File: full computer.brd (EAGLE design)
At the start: 99.9 x 90.2 mm, 74 parts, among them IC2 74HC541N, IC3 74HC573N, IC4 74HC04N, Q1 IRF9530, X1 1503_08

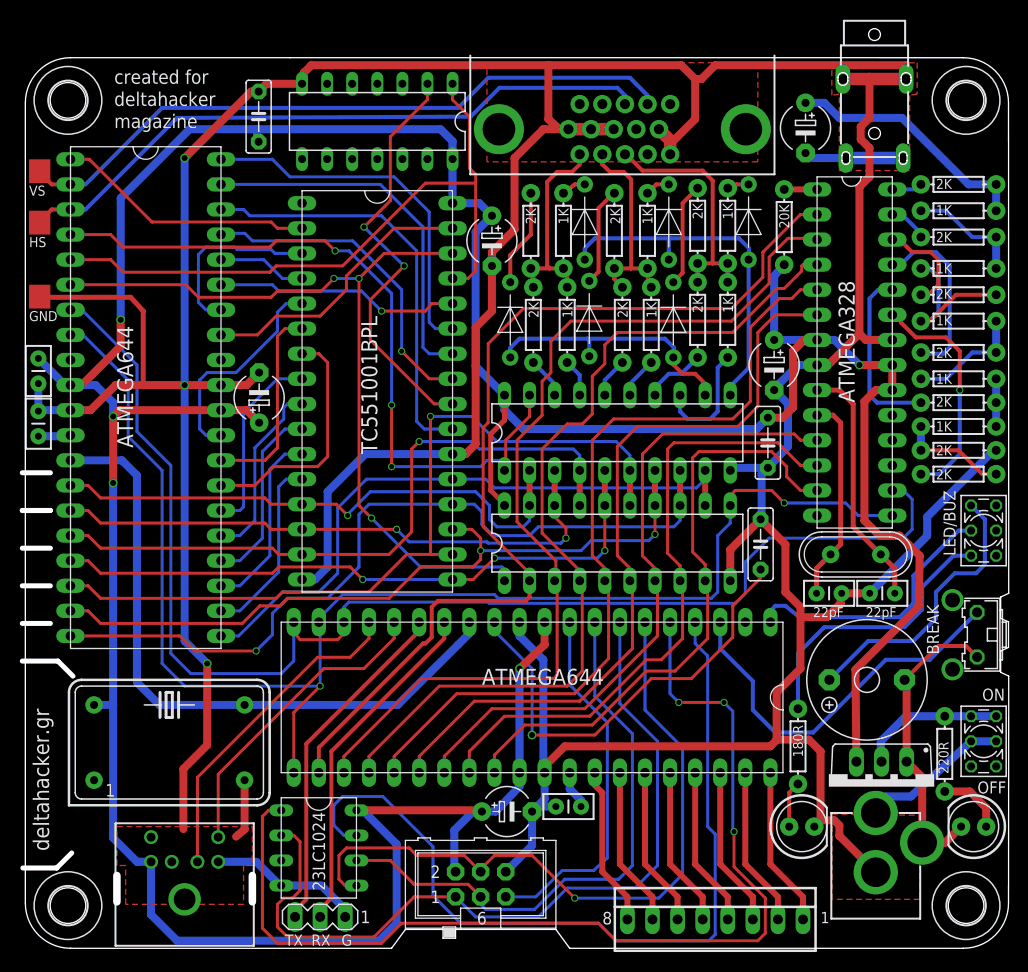
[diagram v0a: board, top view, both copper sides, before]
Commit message: thiner and shorter traces for clock signals, better position for GPIO and SERIAL, schematic clean up
Signed-off-by: Panagiotis Varelas <varelaspanos@gmail.com>
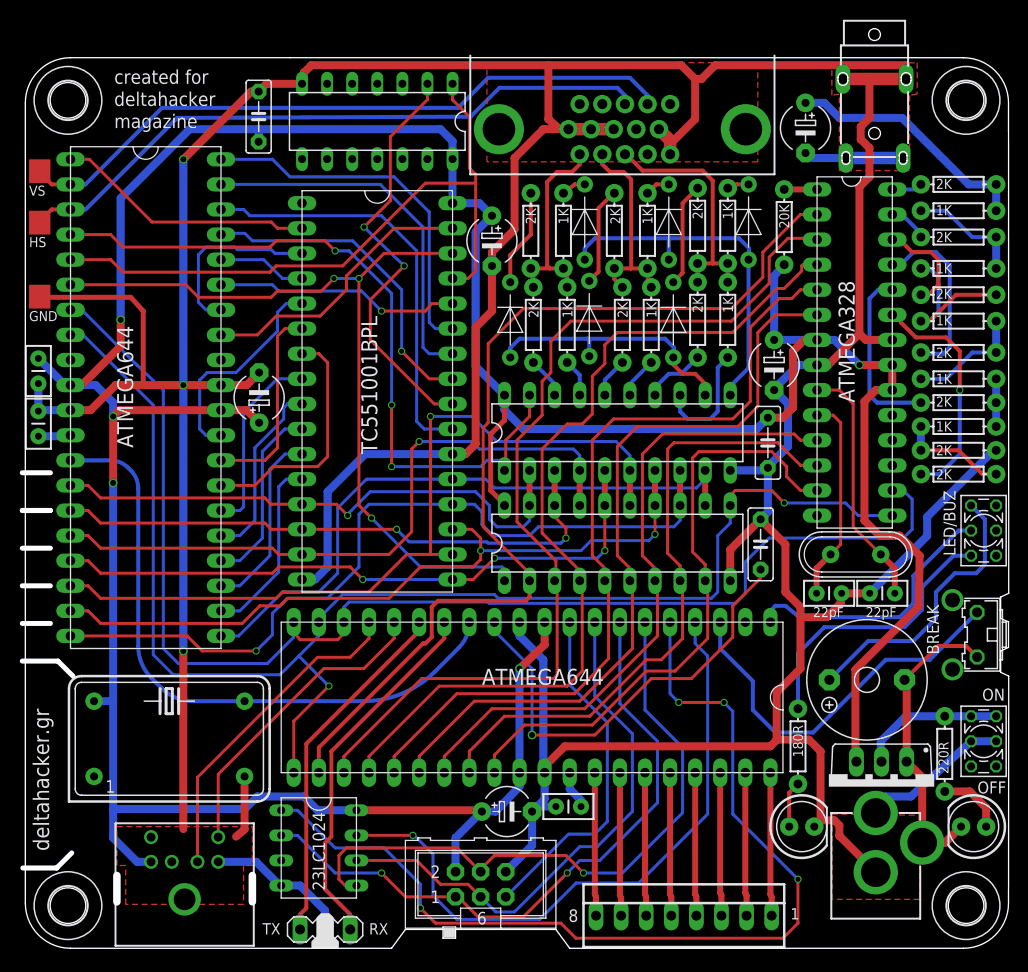
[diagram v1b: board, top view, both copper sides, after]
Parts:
- moved GPIO 3.20 mm to (105.9, 13.5)
- moved JMP1 1.37 mm to (69.6, 12.1)
- moved QG1 0.38 mm to (53.8, 31.4)
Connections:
- net GND: now also JMP1.2; no longer JMP1.1
- net N$22: now also JMP1.1; no longer JMP1.2
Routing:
- net VCC: track 378.7 -> 358.7 mm
- net N$53: track 85.4 -> 65.9 mm, vias 0 -> 1
- net N$50: track 82.1 -> 66.2 mm, vias 0 -> 2
- net N$52: track 105.1 -> 98.3 mm, vias 3 -> 4
- net N$51: track 71.3 -> 65.5 mm
- net N$48: track 58.5 -> 55.1 mm
- net N$1: track 67.1 -> 64.0 mm
- net GND: track 539.2 -> 536.9 mm
- net N$61: track 37.3 -> 35.2 mm
- net N$22: track 35.1 -> 37.2 mm
- net TO_CPU: track 135.0 -> 132.9 mm
- net N$58: track 16.2 -> 14.5 mm
- net N$60: track 16.2 -> 14.5 mm
- net N$55: track 16.2 -> 14.5 mm
- net N$4: track 16.2 -> 14.5 mm
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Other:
- board text removed: "G"
